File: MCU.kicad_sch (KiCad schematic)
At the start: 14 parts, among them U6 STM32F103RBTx, X1 CSTNE8M00G520000R0

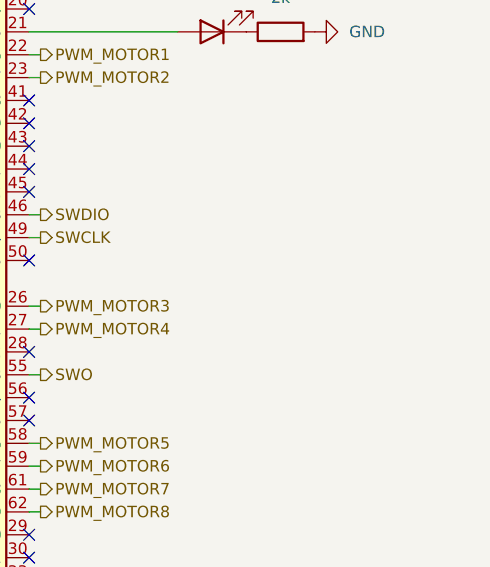
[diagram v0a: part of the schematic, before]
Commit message: add EEPROM funcionality, created new hierarchical sheet
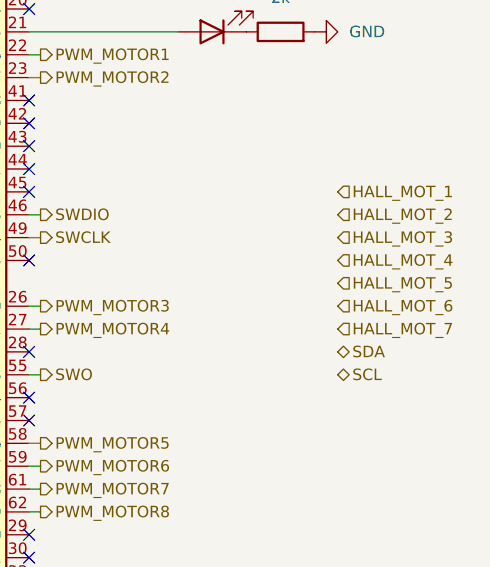
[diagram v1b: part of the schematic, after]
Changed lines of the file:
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@@
+    (effects (font (size 1.27 1.27)) (justify left))
+  )
+  (hierarchical_label "SCL" (shape bidirectional) (at 189.23 116.84 0)
     (effects (font (size 1.27 1.27)) (justify left))
   )
@@
   )
   (hierarchical_label "SPI_SCK" (shape output) (at 160.02 142.24 0)
+    (effects (font (size 1.27 1.27)) (justify left))
+  )
+  (hierarchical_label "HALL_MOT_6" (shape input) (at 189.23 109.22 0)
     (effects (font (size 1.27 1.27)) (justify left))
   )
@@
   )
   (hierarchical_label "PWM_MOTOR1" (shape output) (at 156.21 81.28 0)
+    (effects (font (size 1.27 1.27)) (justify left))
+  )
+  (hierarchical_label "HALL_MOT_5" (shape input) (at 189.23 106.68 0)
+    (effects (font (size 1.27 1.27)) (justify left))
+  )
+  (hierarchical_label "HALL_MOT_2" (shape input) (at 189.23 99.06 0)
     (effects (font (size 1.27 1.27)) (justify left))
   )
@@
     (effects (font (size 1.27 1.27)) (justify right))
   )
+  (hierarchical_label "SDA" (shape bidirectional) (at 189.23 114.3 0)
+    (effects (font (size 1.27 1.27)) (justify left))
+  )
   (hierarchical_label "PWM_MOTOR3" (shape output) (at 156.21 109.22 0)
     (effects (font (size 1.27 1.27)) (justify left))
@@
     (effects (font (size 1.27 1.27)) (justify left))
   )
+  (hierarchical_label "HALL_MOT_4" (shape input) (at 189.23 104.14 0)
+    (effects (font (size 1.27 1.27)) (justify left))
+  )
+  (hierarchical_label "HALL_MOT_3" (shape input) (at 189.23 101.6 0)
+    (effects (font (size 1.27 1.27)) (justify left))
+  )
   (hierarchical_label "ADC1_IN0" (shape input) (at 157.48 66.04 0)
     (effects (font (size 1.27 1.27)) (justify left))
   )
+  (hierarchical_label "HALL_MOT_7" (shape input) (at 189.23 111.76 0)
+    (effects (font (size 1.27 1.27)) (justify left))
+  )
+  (hierarchical_label "HALL_MOT_1" (shape input) (at 189.23 96.52 0)
+    (effects (font (size 1.27 1.27)) (justify left))
+  )

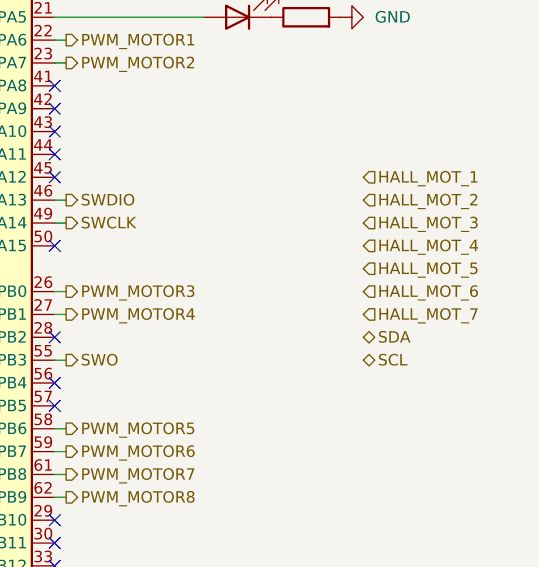
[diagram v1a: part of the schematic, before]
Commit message: added power loss detection, preparing for new pcb layout
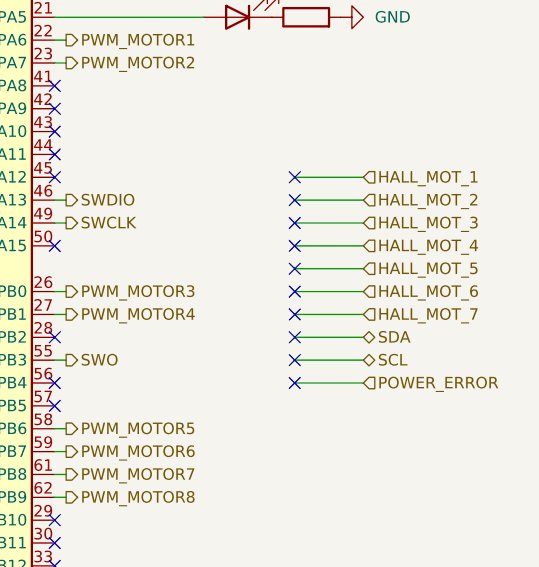
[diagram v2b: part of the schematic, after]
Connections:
- no-connect marks 22 -> 32
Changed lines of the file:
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@@
   (no_connect (at 154.94 96.52))
   (no_connect (at 119.38 139.7))
+  (no_connect (at 181.61 116.84))
+  (no_connect (at 181.61 106.68))
   (no_connect (at 119.38 144.78))
+  (no_connect (at 181.61 99.06))
+  (no_connect (at 181.61 109.22))
   (no_connect (at 154.94 121.92))
   (no_connect (at 154.94 68.58))
+  (no_connect (at 181.61 114.3))
   (no_connect (at 119.38 142.24))
   (no_connect (at 119.38 104.14))
   (no_connect (at 154.94 119.38))
+  (no_connect (at 181.61 111.76))
   (no_connect (at 154.94 134.62))
+  (no_connect (at 181.61 119.38))
   (no_connect (at 119.38 119.38))
   (no_connect (at 119.38 121.92))
   (no_connect (at 154.94 93.98))
+  (no_connect (at 181.61 101.6))
   (no_connect (at 154.94 104.14))
   (no_connect (at 119.38 137.16))
   (no_connect (at 154.94 137.16))
   (no_connect (at 154.94 139.7))
+  (no_connect (at 181.61 96.52))
+  (no_connect (at 181.61 104.14))
   (no_connect (at 154.94 76.2))
   (wire (pts (xy 156.21 73.66) (xy 154.94 73.66))
@@
     (stroke (width 0) (type default) (color 0 0 0 0))
   )
+  (wire (pts (xy 181.61 96.52) (xy 189.23 96.52))
+    (stroke (width 0) (type default) (color 0 0 0 0))
+  )
   (wire (pts (xy 139.7 59.69) (xy 142.24 59.69))
     (stroke (width 0) (type default) (color 0 0 0 0))
@@
     (stroke (width 0) (type default) (color 0 0 0 0))
   )
+  (wire (pts (xy 181.61 116.84) (xy 189.23 116.84))
+    (stroke (width 0) (type default) (color 0 0 0 0))
+  )
+  (wire (pts (xy 181.61 106.68) (xy 189.23 106.68))
+    (stroke (width 0) (type default) (color 0 0 0 0))
+  )
   (wire (pts (xy 160.02 142.24) (xy 154.94 142.24))
     (stroke (width 0) (type default) (color 0 0 0 0))
@@
     (stroke (width 0) (type default) (color 0 0 0 0))
   )
+  (wire (pts (xy 181.61 99.06) (xy 189.23 99.06))
+    (stroke (width 0) (type default) (color 0 0 0 0))
+  )
   (wire (pts (xy 113.03 78.74) (xy 115.57 78.74))
     (stroke (width 0) (type default) (color 0 0 0 0))
@@
     (stroke (width 0) (type default) (color 0 0 0 0))
   )
+  (wire (pts (xy 181.61 109.22) (xy 189.23 109.22))
+    (stroke (width 0) (type default) (color 0 0 0 0))
+  )
   (wire (pts (xy 138.43 40.64) (xy 138.43 43.18))
     (stroke (width 0) (type default) (color 0 0 0 0))
@@
     (stroke (width 0) (type default) (color 0 0 0 0))
   )
+  (wire (pts (xy 181.61 114.3) (xy 189.23 114.3))
+    (stroke (width 0) (type default) (color 0 0 0 0))
+  )
   (wire (pts (xy 118.11 95.25) (xy 118.11 99.06))
     (stroke (width 0) (type default) (color 0 0 0 0))
@@
     (stroke (width 0) (type default) (color 0 0 0 0))
   )
+  (wire (pts (xy 181.61 111.76) (xy 189.23 111.76))
+    (stroke (width 0) (type default) (color 0 0 0 0))
+  )
   (wire (pts (xy 156.21 83.82) (xy 154.94 83.82))
     (stroke (width 0) (type default) (color 0 0 0 0))
@@
     (stroke (width 0) (type default) (color 0 0 0 0))
   )
+  (wire (pts (xy 181.61 101.6) (xy 189.23 101.6))
+    (stroke (width 0) (type default) (color 0 0 0 0))
+  )
   (wire (pts (xy 118.11 99.06) (xy 119.38 99.06))
     (stroke (width 0) (type default) (color 0 0 0 0))
@@
     (stroke (width 0) (type default) (color 0 0 0 0))
   )
+  (wire (pts (xy 181.61 119.38) (xy 189.23 119.38))
+    (stroke (width 0) (type default) (color 0 0 0 0))
+  )
   (wire (pts (xy 96.52 64.77) (xy 96.52 66.04))
     (stroke (width 0) (type default) (color 0 0 0 0))
@@
     (stroke (width 0) (type default) (color 0 0 0 0))
   )
+  (wire (pts (xy 181.61 104.14) (xy 189.23 104.14))
+    (stroke (width 0) (type default) (color 0 0 0 0))
+  )
   (wire (pts (xy 111.76 43.18) (xy 120.65 43.18))
     (stroke (width 0) (type default) (color 0 0 0 0))
@@
     (effects (font (size 1.27 1.27)) (justify left))
   )
+  (hierarchical_label "POWER_ERROR" (shape input) (at 189.23 119.38 0)
+    (effects (font (size 1.27 1.27)) (justify left))
+  )

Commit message: pcb is in progress, finishing H-bridge layout
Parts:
- C15, C16, C17, C18, C19, C20, C21: footprint Capacitor_SMD:C_0603_1608Metric -> Capacitor_SMD:C_0603_1608Metric_Pad1.08x0.95mm_HandSolder
- R10, R11: footprint Resistor_SMD:R_0603_1608Metric -> Resistor_SMD:R_0603_1608Metric_Pad0.98x0.95mm_HandSolder
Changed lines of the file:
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@@
     (property "Reference" "R11" (id 0) (at 182.88 72.39 90))
     (property "Value" "2k" (id 1) (at 182.88 74.93 90))
-    (property "Footprint" "Resistor_SMD:R_0603_1608Metric" (id 2) (at 182.88 80.518 90)
+    (property "Footprint" "Resistor_SMD:R_0603_1608Metric_Pad0.98x0.95mm_HandSolder" (id 2) (at 182.88 80.518 90)
       (effects (font (size 1.27 1.27)) hide)
     )
@@
       (effects (font (size 1.27 1.27)) (justify left))
     )
-    (property "Footprint" "Capacitor_SMD:C_0603_1608Metric" (id 2) (at 148.2852 40.64 0)
+    (property "Footprint" "Capacitor_SMD:C_0603_1608Metric_Pad1.08x0.95mm_HandSolder" (id 2) (at 148.2852 40.64 0)
       (effects (font (size 1.27 1.27)) hide)
     )
@@
       (effects (font (size 1.27 1.27)) (justify left))
     )
-    (property "Footprint" "Capacitor_SMD:C_0603_1608Metric" (id 2) (at 97.4852 74.93 0)
+    (property "Footprint" "Capacitor_SMD:C_0603_1608Metric_Pad1.08x0.95mm_HandSolder" (id 2) (at 97.4852 74.93 0)
       (effects (font (size 1.27 1.27)) hide)
     )
@@
       (effects (font (size 1.27 1.27)) (justify left))
     )
-    (property "Footprint" "Capacitor_SMD:C_0603_1608Metric" (id 2) (at 121.6152 40.64 0)
+    (property "Footprint" "Capacitor_SMD:C_0603_1608Metric_Pad1.08x0.95mm_HandSolder" (id 2) (at 121.6152 40.64 0)
       (effects (font (size 1.27 1.27)) hide)
     )
@@
       (effects (font (size 1.27 1.27)) (justify left))
     )
-    (property "Footprint" "Capacitor_SMD:C_0603_1608Metric" (id 2) (at 130.5052 40.64 0)
+    (property "Footprint" "Capacitor_SMD:C_0603_1608Metric_Pad1.08x0.95mm_HandSolder" (id 2) (at 130.5052 40.64 0)
       (effects (font (size 1.27 1.27)) hide)
     )
@@
       (effects (font (size 1.27 1.27)) (justify left))
     )
-    (property "Footprint" "Capacitor_SMD:C_0603_1608Metric" (id 2) (at 157.1752 40.64 0)
+    (property "Footprint" "Capacitor_SMD:C_0603_1608Metric_Pad1.08x0.95mm_HandSolder" (id 2) (at 157.1752 40.64 0)
       (effects (font (size 1.27 1.27)) hide)
     )
@@
       (effects (font (size 1.27 1.27)) (justify left))
     )
-    (property "Footprint" "Capacitor_SMD:C_0603_1608Metric" (id 2) (at 112.7252 40.64 0)
+    (property "Footprint" "Capacitor_SMD:C_0603_1608Metric_Pad1.08x0.95mm_HandSolder" (id 2) (at 112.7252 40.64 0)
       (effects (font (size 1.27 1.27)) hide)
     )
@@
       (effects (font (size 1.27 1.27)) (justify left))
     )
-    (property "Footprint" "Capacitor_SMD:C_0603_1608Metric" (id 2) (at 139.3952 40.64 0)
+    (property "Footprint" "Capacitor_SMD:C_0603_1608Metric_Pad1.08x0.95mm_HandSolder" (id 2) (at 139.3952 40.64 0)
       (effects (font (size 1.27 1.27)) hide)
     )
@@
       (effects (font (size 1.27 1.27)) (justify left))
     )
-    (property "Footprint" "Resistor_SMD:R_0603_1608Metric" (id 2) (at 94.742 60.96 90)
-      (effects (font (size 1.27 1.27)) hide)
-    )
+    (property "Footprint" "Resistor_SMD:R_0603_1608Metric_Pad0.98x0.95mm_HandSolder" (id 2) (at 94.742 60.96 90)
+      (effects (font (size 1.27 1.27)) hide)
+    )
